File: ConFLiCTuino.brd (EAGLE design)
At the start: 99.1 x 53.3 mm, 73 parts, among them IC4 LM358D, J1 Power, Q1 IRLR024N, Q2 BC847B, Q3 BC847B, Q5 IRLR024N, Q6 IRLR024N, Q7 IRF9Z34NS, Q8 IRF9Z34NS

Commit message: init V0.3
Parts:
- D1, D3: value 1N400X -> S1D; device diode:MELF-MLL41 -> diode:DO214AC
- moved D1 1.91 mm to (15.2, 20.3)
- moved D3 1.90 mm to (15.2, 10.8)
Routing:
- net GND: track 112.4 -> 109.3 mm
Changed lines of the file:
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@@
 <setting verticaltext="up"/>
 </settings>
-<grid distance="12.5" unitdist="mil" unit="mm" style="lines" multiple="1" display="no" altdistance="6.25" altunitdist="mil" altunit="mil"/>
+<grid distance="12.5" unitdist="mil" unit="mil" style="lines" multiple="1" display="no" altdistance="6.25" altunitdist="mil" altunit="mil"/>
 <layers>
 <layer number="1" name="Top" color="4" fill="1" visible="yes" active="yes"/>
@@
 <layer number="20" name="Dimension" color="15" fill="1" visible="yes" active="yes"/>
 <layer number="21" name="tPlace" color="7" fill="1" visible="yes" active="yes"/>
-<layer number="22" name="bPlace" color="7" fill="1" visible="no" active="yes"/>
-<layer number="23" name="tOrigins" color="15" fill="1" visible="no" active="yes"/>
-<layer number="24" name="bOrigins" color="15" fill="1" visible="no" active="yes"/>
-<layer number="25" name="tNames" color="7" fill="1" visible="yes" active="yes"/>
+<layer number="22" name="bPlace" color="7" fill="1" visible="yes" active="yes"/>
+<layer number="23" name="tOrigins" color="15" fill="1" visible="yes" active="yes"/>
+<layer number="24" name="bOrigins" color="15" fill="1" visible="yes" active="yes"/>
+<layer number="25" name="tNames" color="7" fill="1" visible="no" active="yes"/>
 <layer number="26" name="bNames" color="7" fill="1" visible="no" active="yes"/>
 <layer number="27" name="tValues" color="7" fill="1" visible="no" active="yes"/>
@@
 <layer number="47" name="Measures" color="7" fill="1" visible="no" active="yes"/>
 <layer number="48" name="Document" color="7" fill="1" visible="yes" active="yes"/>
-<layer number="49" name="Reference" color="7" fill="1" visible="no" active="yes"/>
+<layer number="49" name="Reference" color="7" fill="1" visible="yes" active="yes"/>
 <layer number="50" name="dxf" color="7" fill="1" visible="no" active="no"/>
-<layer number="51" name="tDocu" color="7" fill="1" visible="no" active="yes"/>
-<layer number="52" name="bDocu" color="7" fill="1" visible="no" active="yes"/>
+<layer number="51" name="tDocu" color="7" fill="1" visible="yes" active="yes"/>
+<layer number="52" name="bDocu" color="7" fill="1" visible="yes" active="yes"/>
 <layer number="91" name="Nets" color="2" fill="1" visible="no" active="no"/>
 <layer number="92" name="Busses" color="1" fill="1" visible="no" active="no"/>
@@
 <attribute name="VALUE" x="24.13" y="23.495" size="1.27" layer="27"/>
 </element>
-<element name="D1" library="diode" package="MELF-MLL41" value="1N400X" x="15.24" y="22.225" smashed="yes" rot="R90">
-<attribute name="NAME" x="17.599" y="22.983" size="1.016" layer="25" rot="R270"/>
-<attribute name="VALUE" x="18.234" y="19.562" size="1.27" layer="27" rot="R90"/>
-</element>
-<element name="D3" library="diode" package="MELF-MLL41" value="1N400X" x="15.24" y="12.7" smashed="yes" rot="R90">
-<attribute name="NAME" x="17.599" y="13.458" size="1.016" layer="25" rot="R270"/>
-<attribute name="VALUE" x="18.234" y="10.037" size="1.27" layer="27" rot="R90"/>
+<element name="D1" library="diode" package="DO214AC" value="S1D" x="15.24" y="20.32" smashed="yes" rot="R90">
+<attribute name="NAME" x="17.599" y="21.078" size="1.016" layer="25" rot="R270"/>
+<attribute name="VALUE" x="18.234" y="17.657" size="1.27" layer="27" rot="R90"/>
+</element>
+<element name="D3" library="diode" package="DO214AC" value="S1D" x="15.24" y="10.795" smashed="yes" rot="R90">
+<attribute name="NAME" x="17.599" y="11.553" size="1.016" layer="25" rot="R270"/>
+<attribute name="VALUE" x="18.234" y="8.132" size="1.27" layer="27" rot="R90"/>
 </element>
 <element name="LED" library="pinhead" package="2X04" value="" x="78.105" y="27.94" smashed="yes" rot="R270">
@@
 <via x="35.56" y="44.45" extent="1-16" drill="0.4"/>
 <wire x1="10.4775" y1="22.225" x2="3.175" y2="22.225" width="1.4224" layer="1"/>
-<wire x1="10.4775" y1="22.225" x2="14.605" y2="22.225" width="1.4224" layer="1"/>
-<wire x1="14.605" y1="22.225" x2="15.24" y2="22.86" width="1.4224" layer="1"/>
-<wire x1="15.24" y1="22.86" x2="15.24" y2="24.85" width="1.4224" layer="1"/>
 <wire x1="10.4775" y1="12.7" x2="3.175" y2="12.7" width="1.4224" layer="1"/>
-<wire x1="10.4775" y1="12.7" x2="12.7" y2="12.7" width="1.4224" layer="1"/>
-<wire x1="12.7" y1="12.7" x2="15.24" y2="15.24" width="1.4224" layer="1"/>
-<wire x1="15.24" y1="15.24" x2="15.24" y2="15.325" width="1.4224" layer="1"/>
 <wire x1="24.45" y1="26.035" x2="23.01875" y2="26.035" width="0.4064" layer="1"/>
 <via x="23.01875" y="26.035" extent="1-16" drill="0.4"/>
@@
 <via x="76.5175" y="43.4975" extent="1-16" drill="0.4"/>
 <via x="80.9625" y="43.4975" extent="1-16" drill="0.4"/>
+<wire x1="15.24" y1="22.37" x2="15.24" y2="22.225" width="1.4224" layer="1"/>
+<wire x1="15.24" y1="22.225" x2="10.4775" y2="22.225" width="1.4224" layer="1"/>
+<wire x1="15.24" y1="12.845" x2="15.24" y2="12.7" width="1.4224" layer="1"/>
+<wire x1="15.24" y1="12.7" x2="10.4775" y2="12.7" width="1.4224" layer="1"/>
 </signal>
 <signal name="+3V3">

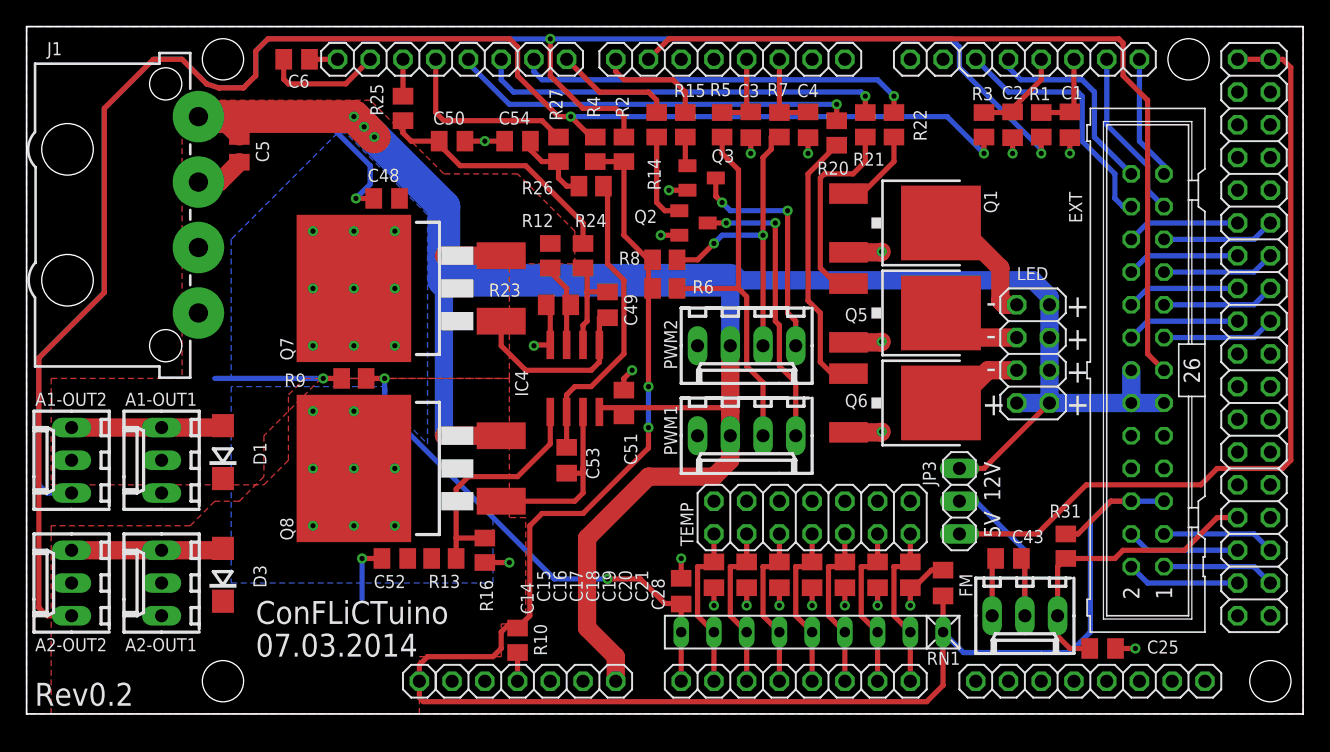
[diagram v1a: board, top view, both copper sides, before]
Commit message: Init V0.4
Changed whole layout. More resistor nets and smaller board.
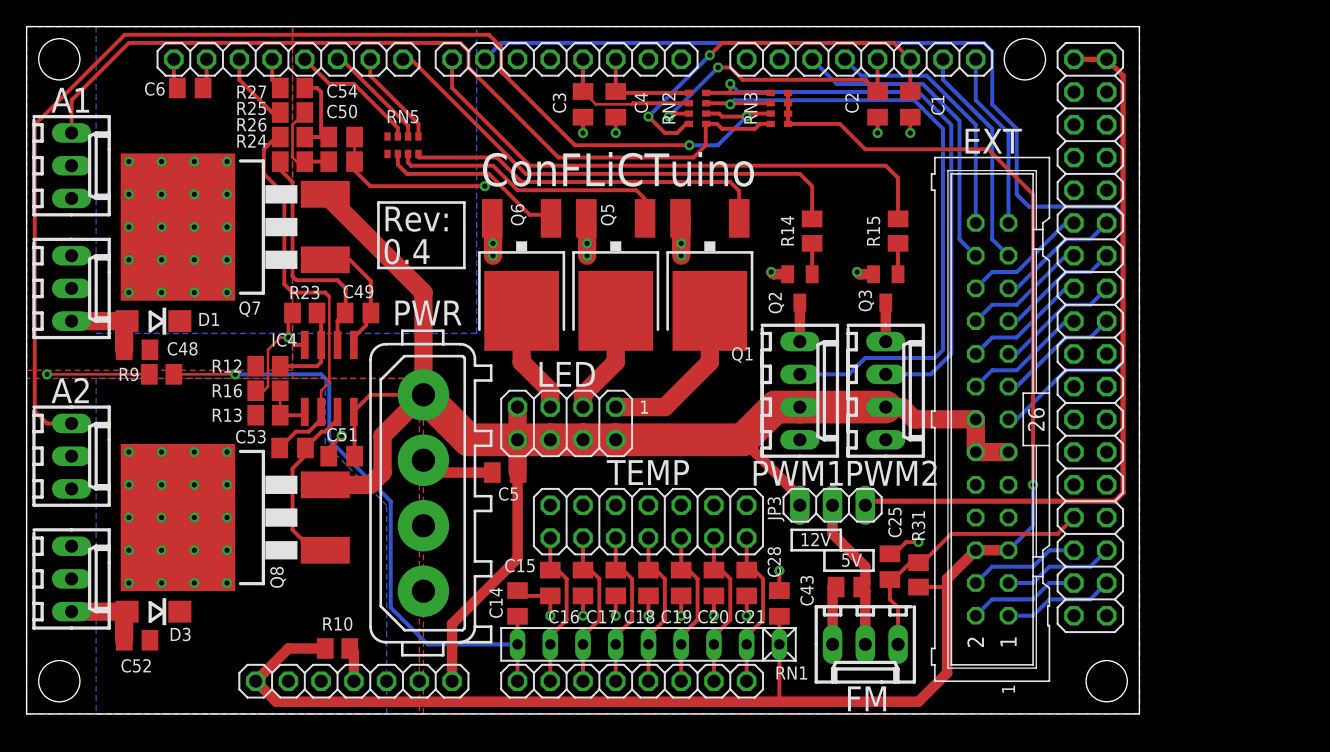
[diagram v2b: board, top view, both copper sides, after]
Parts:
- removed J1: Power, con-amp:827001
- removed JP1: (no value), pinhead:1X01
- removed R1, R3, R5, R7: 10k, rcl:M0805
- removed R2, R4, R6, R8: 4k7, rcl:M0805
- removed R20, R21, R22: 180, rcl:M0805
- added PWR: (no value), con-amp:350211
- added RN2: 10K, resistor-dil:CAT16
- added RN3: 4k7, resistor-dil:CAT16
- added RN5: 220, resistor-dil:CAT16
- C49, C53: value 10p -> 22p
- IC1: value (none) -> MEGAARDUINO_CUSTOM; device arduino:MEGA_ARDUINO_3 -> arduino:ARDUINO_MEGA_R3_SMALL_CUSTOM
- moved LED 36.6 mm to (41.9, 22.5), turned to 180 degrees
- moved C5 32.5 mm to (37.1, 18.7), turned to 180 degrees
- moved Q6 31.6 mm to (38.4, 33.7), turned to 180 degrees
- moved R24 23.7 mm to (20.6, 42.9), turned to 180 degrees
- moved R12 23.5 mm to (18.7, 27.0), turned to 180 degrees
- moved R26 23.5 mm to (20.6, 44.8)
- moved Q5 23.0 mm to (45.7, 33.7), turned to 180 degrees
- moved A1-OUT2 22.9 mm to (3.49, 42.5), turned to 270 degrees
- moved C48 22.7 mm to (8.57, 28.3)
- moved C51 22.3 mm to (24.4, 20.0), turned to 180 degrees
- moved C53 21.3 mm to (20.6, 20.6), turned to 0 degrees
- moved R27 21.2 mm to (20.6, 48.6), turned to 0 degrees
- moved C52 21.0 mm to (8.57, 5.71)
- moved R16 20.9 mm to (18.7, 25.1), turned to 0 degrees
- moved R23 19.7 mm to (21.6, 31.1)
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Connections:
- new net N$44: C6.2, IC1.45
- net +12V: now also PWR.1; no longer J1.1
- net GND: now also C54.1, PWR.2, PWR.3; no longer C54.2, C6.2, IC1.45, J1.2, J1.3
- net LED_1: now also RN5.5; no longer R22.2
- net LED_2: now also RN5.6; no longer R21.2
- net LED_3: now also RN5.7; no longer R20.2
- net N$12: now also RN2.7, RN3.6; no longer R5.1, R6.1
- net N$14: now also RN2.8, RN3.5; no longer R7.1, R8.1
- net N$2: now also RN2.5, RN3.8; no longer R1.1, R2.1
- net N$5: now also RN2.6, RN3.7; no longer R3.1, R4.1
- net N$53: now also R26.1; no longer R26.2
- net N$54: now also C54.2, R26.2; no longer C54.1, R26.1
- net N$82: now also RN5.2; no longer R20.1
- net N$83: now also RN5.3; no longer R21.1
- net N$84: now also RN5.4; no longer R22.1
- net T_A_1: now also RN2.4; no longer R1.2
- net T_A_2: now also RN2.3; no longer R3.2
- net T_PWM_1: now also RN2.2; no longer R5.2
- net T_PWM_2: now also RN2.1; no longer R7.2
- net V+: now also IC1.0, RN3.1, RN3.2, RN3.3, RN3.4; no longer JP1.1, R2.2, R4.2, R6.2, R8.2
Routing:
- net N$2: track 129.5 -> 65.4 mm, vias 2 -> 0
- net +12V: track 184.5 -> 121.5 mm, vias 5 -> 0
- net PWM_2: track 8.60 -> 42.9 mm
- net N$5: track 125.8 -> 94.4 mm
- net PWM_1: track 9.26 -> 38.4 mm
- net LED_1: track 31.0 -> 7.54 mm, vias 1 -> 0
- net T_A_1: track 6.45 -> 29.7 mm, vias 0 -> 2
- net LED_2: track 31.6 -> 8.45 mm, vias 1 -> 0
- net N$14: track 24.6 -> 47.7 mm, vias 2 -> 1
- net N$12: track 29.6 -> 51.7 mm, vias 0 -> 1
- net N$84: track 6.51 -> 28.3 mm
- net LED_3: track 31.5 -> 10.1 mm, vias 1 -> 0
- net N$22: track 22.4 -> 3.03 mm, vias 2 -> 0
- net N$41: track 64.3 -> 83.1 mm
- net GND: track 109.3 -> 90.9 mm
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- added copper zone on layer 16, net N$42
- added copper zone on layer 1, net N$45
- removed copper zone on layer 1, net BLA
- removed copper zone on layer 16, net N$20
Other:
- board size 99.1 x 53.3 mm -> 86.4 x 53.3 mm
- board text added: "0.4"
- board text added: "1"
- board text added: "A1"
- board text added: "A2"
- board text added: "ConFLiCTuino is a"
- board text added: "Controller For Liquid Cooled Technique"
- board text added: "GND"
- board text added: "Layout by R. Steigemann"
- board text added: "MISO"
- board text added: "MOSI"
- board text added: "PC0"
- board text added: "PC1"
- board text added: "PC2"
- board text added: "PC3"
- board text added: "PC4"
- board text added: "PC5"
- board text added: "PC6"
- board text added: "PC7"
- board text added: "PWM"
- board text added: "PWR"
- board text added: "RXD2"
- board text added: "Rev:"
- board text added: "SCK"
- board text added: "SCL"
- board text added: "SDA"
- board text added: "SS"
- board text added: "Sig."
- board text added: "TXD2"
- board text added: "Ta."
- board text added: "V+"
- board text added: "open-conflict.de"
- board text added: "shield for Arduino Mega."
- board text added: "to GND"
- board text removed: "-"
- board text removed: "07.03.2014"
- board text removed: "Rev0.2"
- board text removed: "don't need to assemble"
- board text removed: "not connected"
